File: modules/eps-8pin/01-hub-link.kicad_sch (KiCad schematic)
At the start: 6 parts, among them J1 TO-HUB

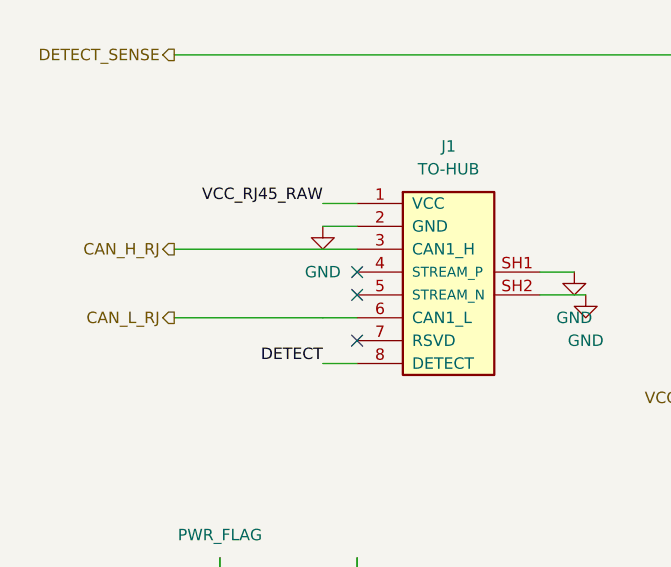
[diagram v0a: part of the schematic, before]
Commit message: Looking through boards and figuring out outlines.
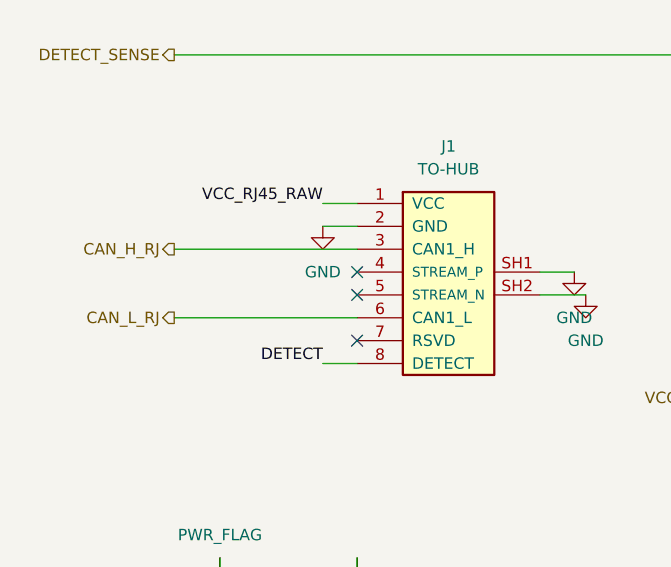
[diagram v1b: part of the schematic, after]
